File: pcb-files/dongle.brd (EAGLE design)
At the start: 100 x 80 mm, 0 parts

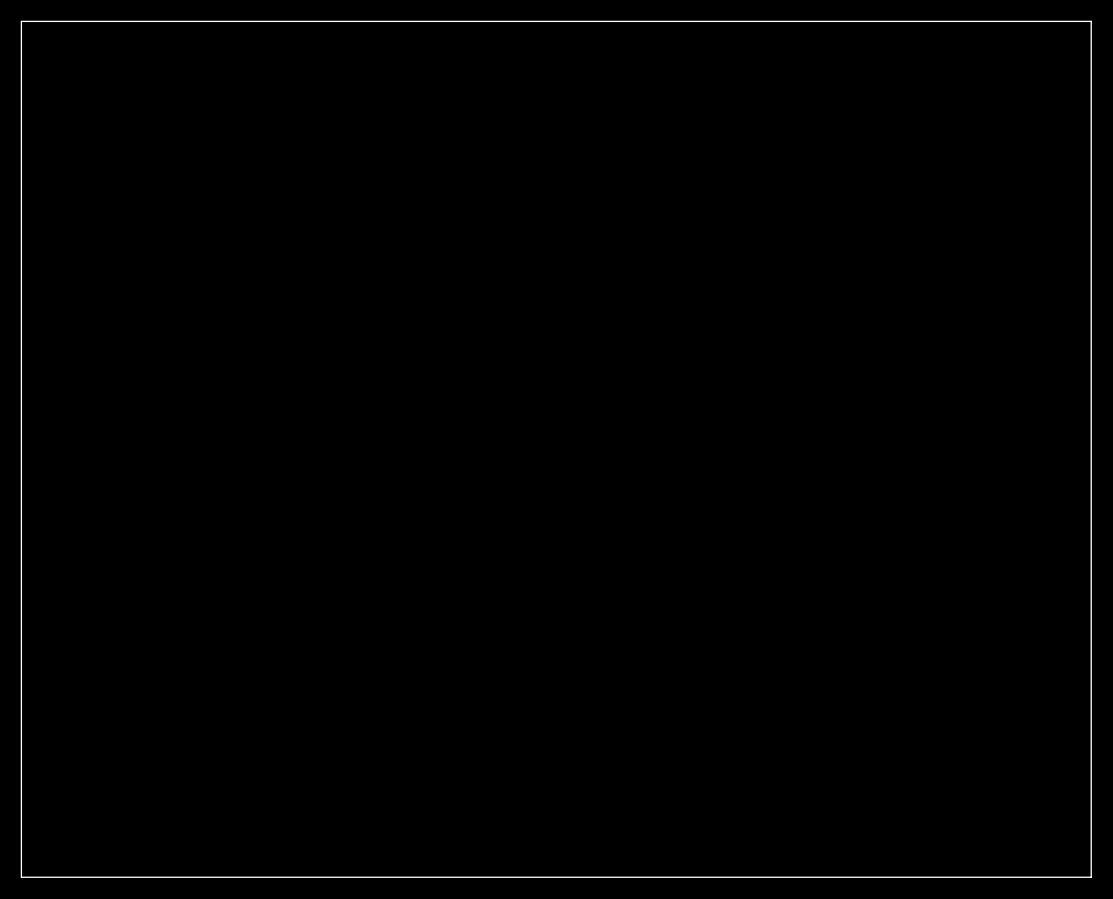
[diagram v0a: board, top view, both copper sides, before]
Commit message: Add finished PCB and BOM
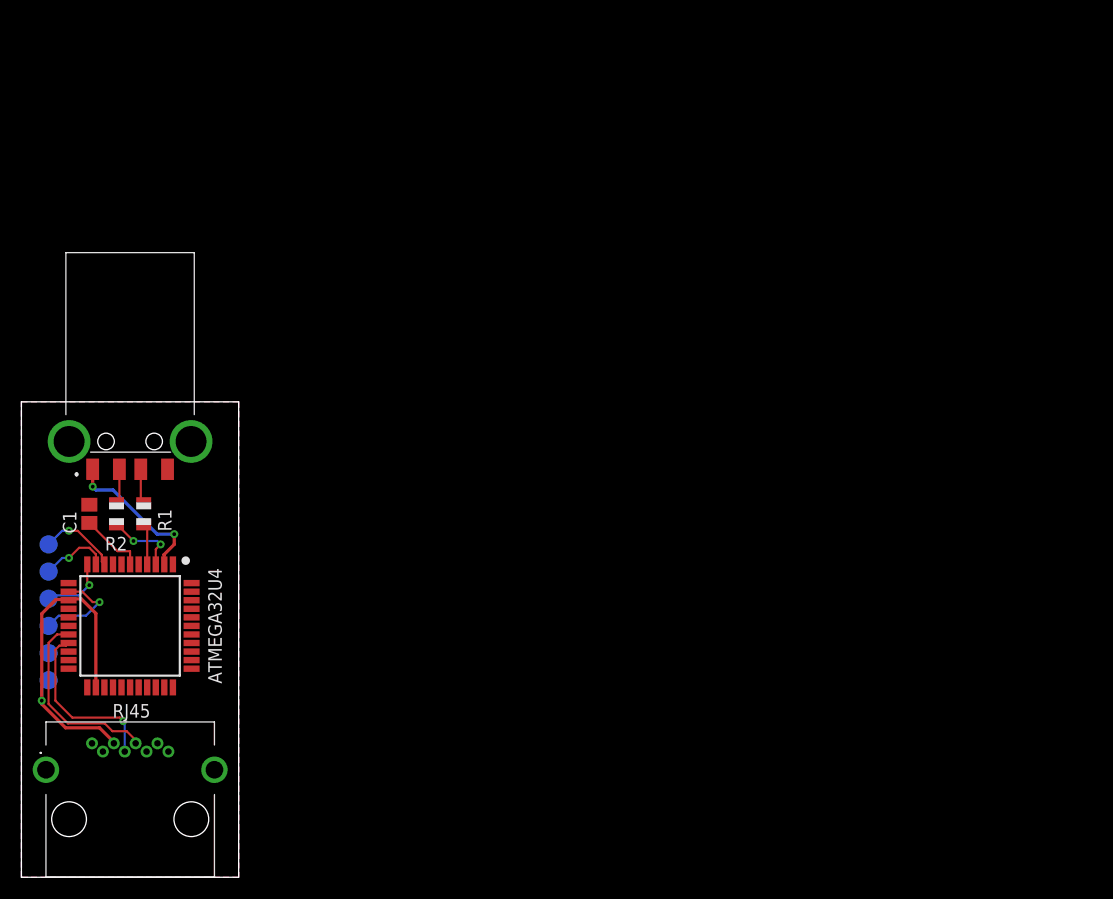
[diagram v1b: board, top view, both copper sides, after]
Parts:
- added 5V, GND, MISO, MOSI, RST, SCLK: TPTP17R, testpad:TP17R
- added C1: 1uF, adafruit:C0805
- added IC1: ATMEGA32U4-AUR, SamacSys_Parts:QFP80P1200X1200X120-44N
- added J1: KUSBX-SMT2AP5S-B, SamacSys_Parts:KUSBXSMT2AP5SB
- added J2: SS-60300-046, SamacSys_Parts:SS60300046
- added R1, R2: 22Ω, adafruit:R0805
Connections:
- new net CLK: IC1.19, J2.5
- new net D+: J1.3, R1.1
- new net D+RES: IC1.4, R1.2
- new net D-: J1.2, R2.1
- new net D-RES: IC1.3, R2.2
- new net DATA: IC1.18, J2.4
- new net GND: C1.2, GND.TP, IC1.15, IC1.5, J1.4, J2.6
- new net MISO: IC1.11, MISO.TP
- new net MOSI: IC1.10, MOSI.TP
- new net RST: IC1.13, RST.TP
- new net SCLK: IC1.9, SCLK.TP
- new net UCAP: C1.1, IC1.6
- new net VCC: 5V.TP, IC1.14, IC1.24, J2.3
- new net VIN: IC1.2, J1.1
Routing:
- net VCC: track 0.00 -> 32.1 mm, vias 0 -> 1
- net DATA: track 0.00 -> 17.7 mm
- net CLK: track 0.00 -> 16.3 mm, vias 0 -> 1
- net VIN: track 0.00 -> 14.3 mm, vias 0 -> 2
- net RST: track 0.00 -> 8.98 mm, vias 0 -> 1
- net SCLK: track 0.00 -> 7.42 mm, vias 0 -> 1
- net D-RES: track 0.00 -> 6.96 mm, vias 0 -> 2
- net MOSI: track 0.00 -> 6.54 mm, vias 0 -> 1
- net MISO: track 0.00 -> 6.35 mm, vias 0 -> 1
- net UCAP: track 0.00 -> 6.14 mm
- net D+RES: track 0.00 -> 3.86 mm
- net D-: track 0.00 -> 3.27 mm
- net D+: track 0.00 -> 3.27 mm
- added copper zone on layer 1, net GND
- added copper zone on layer 16, net GND
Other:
- board size 100 x 80 mm -> 20.3 x 44.4 mm
- board text added: "ATMEGA32U4"
- board text added: "RJ45"
